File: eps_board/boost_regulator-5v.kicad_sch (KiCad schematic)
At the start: 2 parts

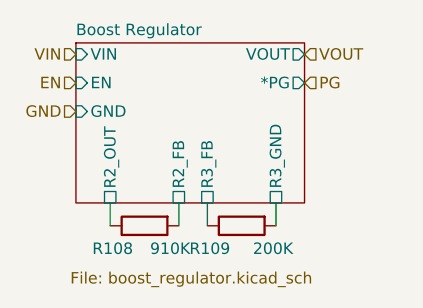
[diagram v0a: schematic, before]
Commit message: add 2V8 regulator and switch for SCI cameras, refactor switch/monitors with nonstandard voltage that require level shifting
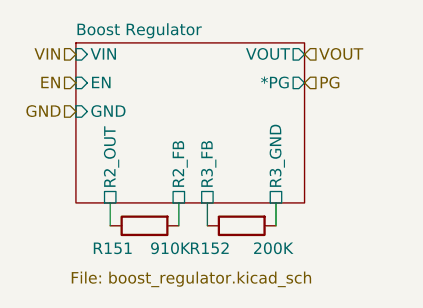
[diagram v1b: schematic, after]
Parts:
- renumbered R108 to R151, R109 to R152
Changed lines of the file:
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@@
 		(on_board yes)
 		(dnp no)
-		(property "Reference" "R108"
+		(property "Reference" "R151"
 			(at 69.8499 72.39 90)
 			(effects
@@
 			(project "EPS"
 				(path "/05170af6-30ef-4c3a-b972-f098085da1bc/687c1244-a40f-4ea6-a397-edb054278cad"
-					(reference "R108")
+					(reference "R151")
 					(unit 1)
 				)
 				(path "/05170af6-30ef-4c3a-b972-f098085da1bc/92098451-3a27-4684-bd37-f9eb10b34fd4"
-					(reference "R81")
+					(reference "R153")
 					(unit 1)
 				)
@@
 		(on_board yes)
 		(dnp no)
-		(property "Reference" "R109"
+		(property "Reference" "R152"
 			(at 80.6449 72.39 90)
 			(effects
@@
 			(project "EPS"
 				(path "/05170af6-30ef-4c3a-b972-f098085da1bc/687c1244-a40f-4ea6-a397-edb054278cad"
-					(reference "R109")
+					(reference "R152")
 					(unit 1)
 				)
 				(path "/05170af6-30ef-4c3a-b972-f098085da1bc/92098451-3a27-4684-bd37-f9eb10b34fd4"
-					(reference "R82")
+					(reference "R154")
 					(unit 1)
 				)

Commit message: connect all parallel solar panels to mcu
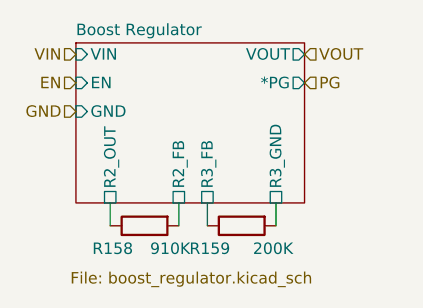
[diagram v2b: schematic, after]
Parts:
- renumbered R151 to R158, R152 to R159
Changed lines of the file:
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@@
 		(on_board yes)
 		(dnp no)
-		(property "Reference" "R151"
+		(property "Reference" "R158"
 			(at 69.8499 72.39 90)
 			(effects
@@
 			(project "EPS"
 				(path "/05170af6-30ef-4c3a-b972-f098085da1bc/687c1244-a40f-4ea6-a397-edb054278cad"
-					(reference "R151")
+					(reference "R158")
 					(unit 1)
 				)
 				(path "/05170af6-30ef-4c3a-b972-f098085da1bc/92098451-3a27-4684-bd37-f9eb10b34fd4"
-					(reference "R153")
+					(reference "R160")
 					(unit 1)
 				)
@@
 		(on_board yes)
 		(dnp no)
-		(property "Reference" "R152"
+		(property "Reference" "R159"
 			(at 80.6449 72.39 90)
 			(effects
@@
 			(project "EPS"
 				(path "/05170af6-30ef-4c3a-b972-f098085da1bc/687c1244-a40f-4ea6-a397-edb054278cad"
-					(reference "R152")
+					(reference "R159")
 					(unit 1)
 				)
 				(path "/05170af6-30ef-4c3a-b972-f098085da1bc/92098451-3a27-4684-bd37-f9eb10b34fd4"
-					(reference "R154")
+					(reference "R161")
 					(unit 1)
 				)

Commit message: flip CAN high low around to ease access from the front side
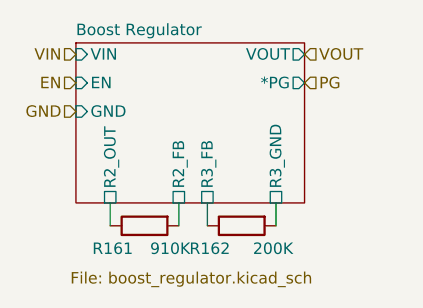
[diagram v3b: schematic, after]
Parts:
- renumbered R158 to R161, R159 to R162
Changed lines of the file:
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@@
 		(on_board yes)
 		(dnp no)
-		(property "Reference" "R158"
+		(property "Reference" "R161"
 			(at 69.8499 72.39 90)
 			(effects
@@
 			(project "EPS"
 				(path "/05170af6-30ef-4c3a-b972-f098085da1bc/687c1244-a40f-4ea6-a397-edb054278cad"
-					(reference "R158")
+					(reference "R161")
 					(unit 1)
 				)
 				(path "/05170af6-30ef-4c3a-b972-f098085da1bc/92098451-3a27-4684-bd37-f9eb10b34fd4"
-					(reference "R160")
+					(reference "R163")
 					(unit 1)
 				)
@@
 		(on_board yes)
 		(dnp no)
-		(property "Reference" "R159"
+		(property "Reference" "R162"
 			(at 80.6449 72.39 90)
 			(effects
@@
 			(project "EPS"
 				(path "/05170af6-30ef-4c3a-b972-f098085da1bc/687c1244-a40f-4ea6-a397-edb054278cad"
-					(reference "R159")
+					(reference "R162")
 					(unit 1)
 				)
 				(path "/05170af6-30ef-4c3a-b972-f098085da1bc/92098451-3a27-4684-bd37-f9eb10b34fd4"
-					(reference "R161")
+					(reference "R164")
 					(unit 1)
 				)

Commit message: replace nearly all buck converters with boost buck (missing is 5raw
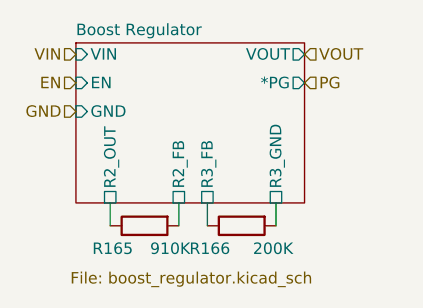
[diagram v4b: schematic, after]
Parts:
- renumbered R161 to R165, R162 to R166
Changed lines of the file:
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@@
 		(on_board yes)
 		(dnp no)
-		(property "Reference" "R161"
+		(property "Reference" "R165"
 			(at 69.8499 72.39 90)
 			(effects
@@
 			(project "EPS"
 				(path "/05170af6-30ef-4c3a-b972-f098085da1bc/687c1244-a40f-4ea6-a397-edb054278cad"
-					(reference "R161")
-					(unit 1)
-				)
-				(path "/05170af6-30ef-4c3a-b972-f098085da1bc/92098451-3a27-4684-bd37-f9eb10b34fd4"
-					(reference "R163")
+					(reference "R165")
 					(unit 1)
 				)
@@
 		(on_board yes)
 		(dnp no)
-		(property "Reference" "R162"
+		(property "Reference" "R166"
 			(at 80.6449 72.39 90)
 			(effects
@@
 			(project "EPS"
 				(path "/05170af6-30ef-4c3a-b972-f098085da1bc/687c1244-a40f-4ea6-a397-edb054278cad"
-					(reference "R162")
-					(unit 1)
-				)
-				(path "/05170af6-30ef-4c3a-b972-f098085da1bc/92098451-3a27-4684-bd37-f9eb10b34fd4"
-					(reference "R164")
+					(reference "R166")
 					(unit 1)
 				)
@@
 					(page "75")
 				)
-				(path "/05170af6-30ef-4c3a-b972-f098085da1bc/92098451-3a27-4684-bd37-f9eb10b34fd4"
-					(page "77")
-				)
-			)
+			)
